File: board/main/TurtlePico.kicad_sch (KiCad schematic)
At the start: 40 parts, among them IC1 DRV8835DSSR, J1 USB-C, J10 LMotor, J11 Micro_SD, J12 FR_ESC, J13 FL_ESC, J14 RR_ESC, J15 RL_ESC, J2 AudioJack3, J3 LED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

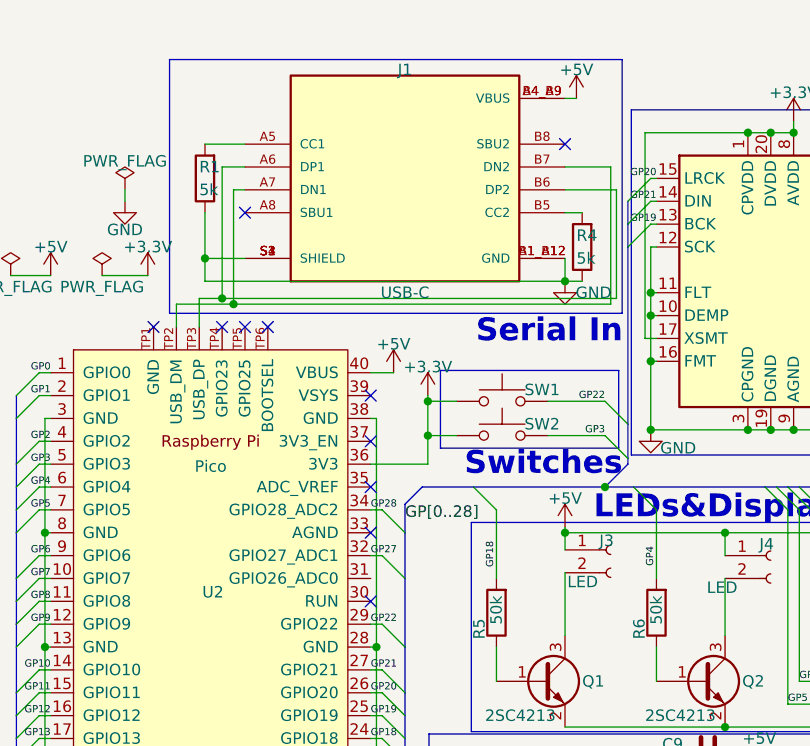
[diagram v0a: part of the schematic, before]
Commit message: add clock function(only digital) in TurtlePico-Dashboard
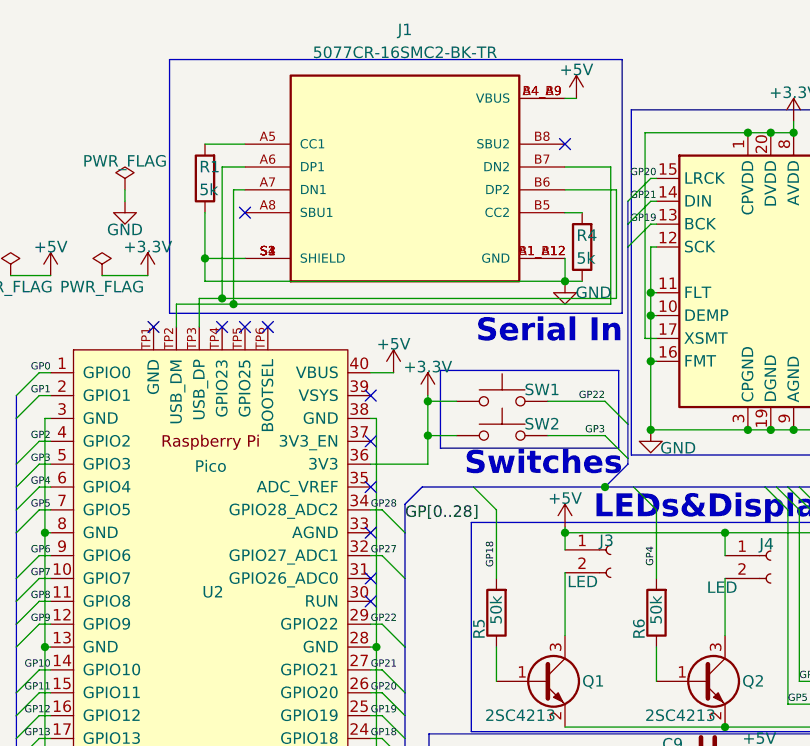
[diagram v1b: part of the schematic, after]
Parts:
- C1, C2: Manufacturer_Name (none) -> Murata Electronics; Manufacturer_Part_Number (none) -> GCM188R71H103KA37J; Mouser Part Number (none) -> 81-GCM188R71H103KA7J; Mouser Price/Stock (none) -> https://www.mouser.jp/ProductDetail/81-GCM188R71H103KA7J
- C10, C9: Manufacturer_Name (none) -> Murata Electronics; Manufacturer_Part_Number (none) -> GCM188R71C104KA37J; Mouser Part Number (none) -> 81-GCM188R71C104KA7J; Mouser Price/Stock (none) -> https://www.mouser.jp/ProductDetail/81-GCM188R71C104KA7J
- C3, C4: Manufacturer_Name (none) -> Murata Electronics; Manufacturer_Part_Number (none) -> GRM188R61H225KE11D; Mouser Part Number (none) -> 81-GRM188R61H225KE1D; Mouser Price/Stock (none) -> https://www.mouser.jp/ProductDetail/81-GRM188R61H225KE1D
- C5, C6, C7, C8: Manufacturer_Name (none) -> Panasonic; Manufacturer_Part_Number (none) -> EEE-FN1A100R; Mouser Part Number (none) -> 667-EEE-FN1A100R; Mouser Price/Stock (none) -> https://www.mouser.jp/ProductDetail/667-EEE-FN1A100R
- IC1: footprint DRV8835:DRV8835DSSR -> DRV8835DSSR; Height 0.8 -> (none)
- J1: value USB-C -> 5077CR-16SMC2-BK-TR; footprint NELTRON_5077CR-16SMC2-BK-TR:NELTRON_5077CR-16SMC2-BK-TR -> NELTRON_5077CR-16SMC2-BK-TR; MANUFACTURER Neltron -> (none); MAXIMUM_PACKAGE_HEIGHT 3.26mm -> (none); Manufacturer_Name (none) -> GCT; Manufacturer_Part_Number (none) -> USB4105-GF-A-060; Mouser Part Number (none) -> 640-USB4105-GF-A-060; Mouser Price/Stock (none) -> https://www.mouser.jp/ProductDetail/GCT/USB4105-GF-A-060?qs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; PARTREV B -> (none); SNAPEDA_PN 5077CR-16SMC2-BK-TR -> (none); STANDARD Manufacturer Recommendations -> (none)
- J11: Manufacturer_Name (none) -> Hirose Connector; Manufacturer_Part_Number (none) -> DM3AT-SF-PEJM5; Mouser Part Number (none) -> 798-DM3AT-SF-PEJM5; Mouser Price/Stock (none) -> https://www.mouser.jp/ProductDetail/Hirose-Connector/DM3AT-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
- J2: footprint Connector_Audio:Jack_3.5mm_Switronic_ST-005-G_horizontal -> STX-3000:STX3000; Manufacturer_Name (none) -> Kycon; Manufacturer_Part_Number (none) -> STX-3000; Mouser Part Number (none) -> 806-STX-3000; Mouser Price/Stock (none) -> https://www.mouser.jp/ProductDetail/Kycon/STX-3000?qs=kjZ2m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
- Q1, Q2: Manufacturer_Name (none) -> Toshiba; Manufacturer_Part_Number (none) -> 2SC4213-A(TE85L,F); Mouser Part Number (none) -> 757-2SC4213-ATE85LF; Mouser Price/Stock (none) -> https://www.mouser.jp/ProductDetail/757-2SC4213-ATE85LF
- R1, R4: Manufacturer_Name (none) -> KOA Speer; Manufacturer_Part_Number (none) -> RN73H1JTTD5101D100; Mouser Part Number (none) -> 660-RN73H1JT5101D100; Mouser Price/Stock (none) -> https://www.mouser.jp/ProductDetail/660-RN73H1JT5101D100
- R2, R3, R7: Manufacturer_Name (none) -> KOA Speer; Manufacturer_Part_Number (none) -> RN73H1JTTD1001F100; Mouser Part Number (none) -> 660-RN73H1JT1001F100; Mouser Price/Stock (none) -> https://www.mouser.jp/ProductDetail/660-RN73H1JT1001F100
- R5, R6: Manufacturer_Name (none) -> KOA Speer; Manufacturer_Part_Number (none) -> RN73H1JTTD5102F100; Mouser Part Number (none) -> 660-RN73H1JT5102F100; Mouser Price/Stock (none) -> https://www.mouser.jp/ProductDetail/660-RN73H1JT5102F100
- R8: Manufacturer_Name (none) -> KOA Speer; Manufacturer_Part_Number (none) -> RN73H1JTTD2001F25; Mouser Part Number (none) -> 660-RN73H1JTD2001F25; Mouser Price/Stock (none) -> https://www.mouser.jp/ProductDetail/660-RN73H1JTD2001F25
- SW1, SW2: Manufacturer_Name (none) -> Alps Alpine; Manufacturer_Part_Number (none) -> SKRPACE010; Mouser Part Number (none) -> 688-SKRPACE010; Mouser Price/Stock (none) -> https://www.mouser.jp/ProductDetail/Alps-Alpine/SKRPACE010?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
- U1: Manufacturer_Name (none) -> Texas Instruments; Manufacturer_Part_Number (none) -> PCM5102APWR; Mouser Part Number (none) -> 595-PCM5102APWR; Mouser Price/Stock (none) -> https://www.mouser.jp/ProductDetail/595-PCM5102APWR
- U2: Manufacturer_Name (none) -> Raspberry Pi; Manufacturer_Part_Number (none) -> SC0918; Mouser Part Number (none) -> 358-SC0918; Mouser Price/Stock (none) -> https://www.mouser.jp/ProductDetail/Raspberry-Pi/SC0918?qs=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
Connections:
- no-connect marks 18 -> 19
